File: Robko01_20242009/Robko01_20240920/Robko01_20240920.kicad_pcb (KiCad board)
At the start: 2 copper layers, 178.8 x 143.8 mm, 70 parts, among them J1 Conn_01x04_Pin, J10 Motors, J11 Motors, J12 Conn_01x04_Pin, J13 Conn_01x02_Pin, J14 Conn_01x04_Pin, J15 Conn_01x02_Pin, J16 Conn_01x04_Pin, J17 Conn_01x02_Male, J18 Conn_01x02_Male, J19 Conn_01x01_Pin, J19 Conn_01x02_Male, J2 Conn_01x02_Pin, J20 Conn_01x01_Pin, J20 Conn_01x02_Male, J21 Conn_01x19_Pin, J22 Conn_01x19_Pin, J23 Conn_01x06_Pin, J24 Conn_01x04_Pin, J25 Conn_01x04_Pin, J26 Conn_01x04_Pin, J27 Conn_01x06_Pin, J28 Conn_01x02_Male, J29 Conn_01x07_Pin, J3 Conn_01x02_Pin, J30 Conn_01x02_Male, J31 Conn_01x02_Male, J4 Conn_01x04_Pin, J5 Conn_01x02_Pin, J6 Conn_01x04_Pin, J7 Conn_01x02_Male, J8 Conn_01x02_Pin, J9 Motors, K2 G5V-2, SW1 SW_DIP_x04, SW2 SW_DIP_x04, SW3 SW_DIP_x04, SW4 SW_DIP_x04, SW5 SW_DIP_x04, SW7 SW_DIP_x04

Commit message: Add more improvements
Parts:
- removed J17, J18, J19, J31: Conn_01x02_Male, Connector_PinHeader_2.54mm:PinHeader_1x02_P2.54mm_Vertical
- removed J19: Conn_01x01_Pin, Connector_PinHeader_2.54mm:PinHeader_1x01_P2.54mm_Vertical
- removed the J20 at (68.0, 108.8)
- added C1: 100nF, Capacitor_THT:C_Disc_D7.5mm_W2.5mm_P5.00mm, F.Cu at (65.3, 113.5)
- added C2: 100nF, Capacitor_THT:C_Disc_D7.5mm_W2.5mm_P5.00mm, F.Cu at (65.3, 118.5)
- added RN1: R_Network04, Resistor_THT:R_Array_SIP5, F.Cu at (107.4, 28.5)
- added U1: LM7805_TO220, Package_TO_SOT_THT:TO-220F-3_Horizontal_TabDown, F.Cu at (70.5, 113.5)
- J30: footprint Connector_PinHeader_2.54mm:PinHeader_1x02_P2.54mm_Vertical -> Connector_PinHeader_2.54mm:PinHeader_1x02_P2.54mm_Horizontal
- moved J30 2.54 mm to (194.6, 106.5), turned to -90 degrees
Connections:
- J21 pad 1: unconnected-(J21-Pin_1-Pad1) -> +3.3V
- J30 pad 1: GRIPPER_2 -> GRIPPER_1
- J30 pad 2: GRIPPER_1 -> GRIPPER_2
- K2 pad 4: Net-(J17-Pin_1) -> GND
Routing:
- net +3.3V: track 0.00 -> 96.9 mm, vias 0 -> 1
- net Net-(J17-Pin_1): track 23.5 -> 0.00 mm
- net VCC: track 276.2 -> 270.7 mm
- net GPIO34: track 82.9 -> 86.6 mm
- net GPIO39: track 82.1 -> 85.8 mm
- net GPIO36: track 81.1 -> 84.8 mm
- net GPIO35: track 83.0 -> 86.7 mm
- net +5V: track 465.3 -> 468.3 mm
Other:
- board text removed: "D-SUN"
- board text removed: "MINI-360"

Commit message: Add E-Stop
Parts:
- added J17: Conn_01x02_Male, Connector_Phoenix_MSTB:PhoenixContact_MSTBA_2,5_2-G-5,08_1x02_P5.08mm_Horizontal, F.Cu at (45.0, 116.0)
- moved J20 50.9 mm to (86.0, 83.6), turned to 90 degrees
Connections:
- net VCC renamed MC_POWER
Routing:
- net MC_POWER: track 270.7 -> 302.0 mm
- net GND: vias 174 -> 176

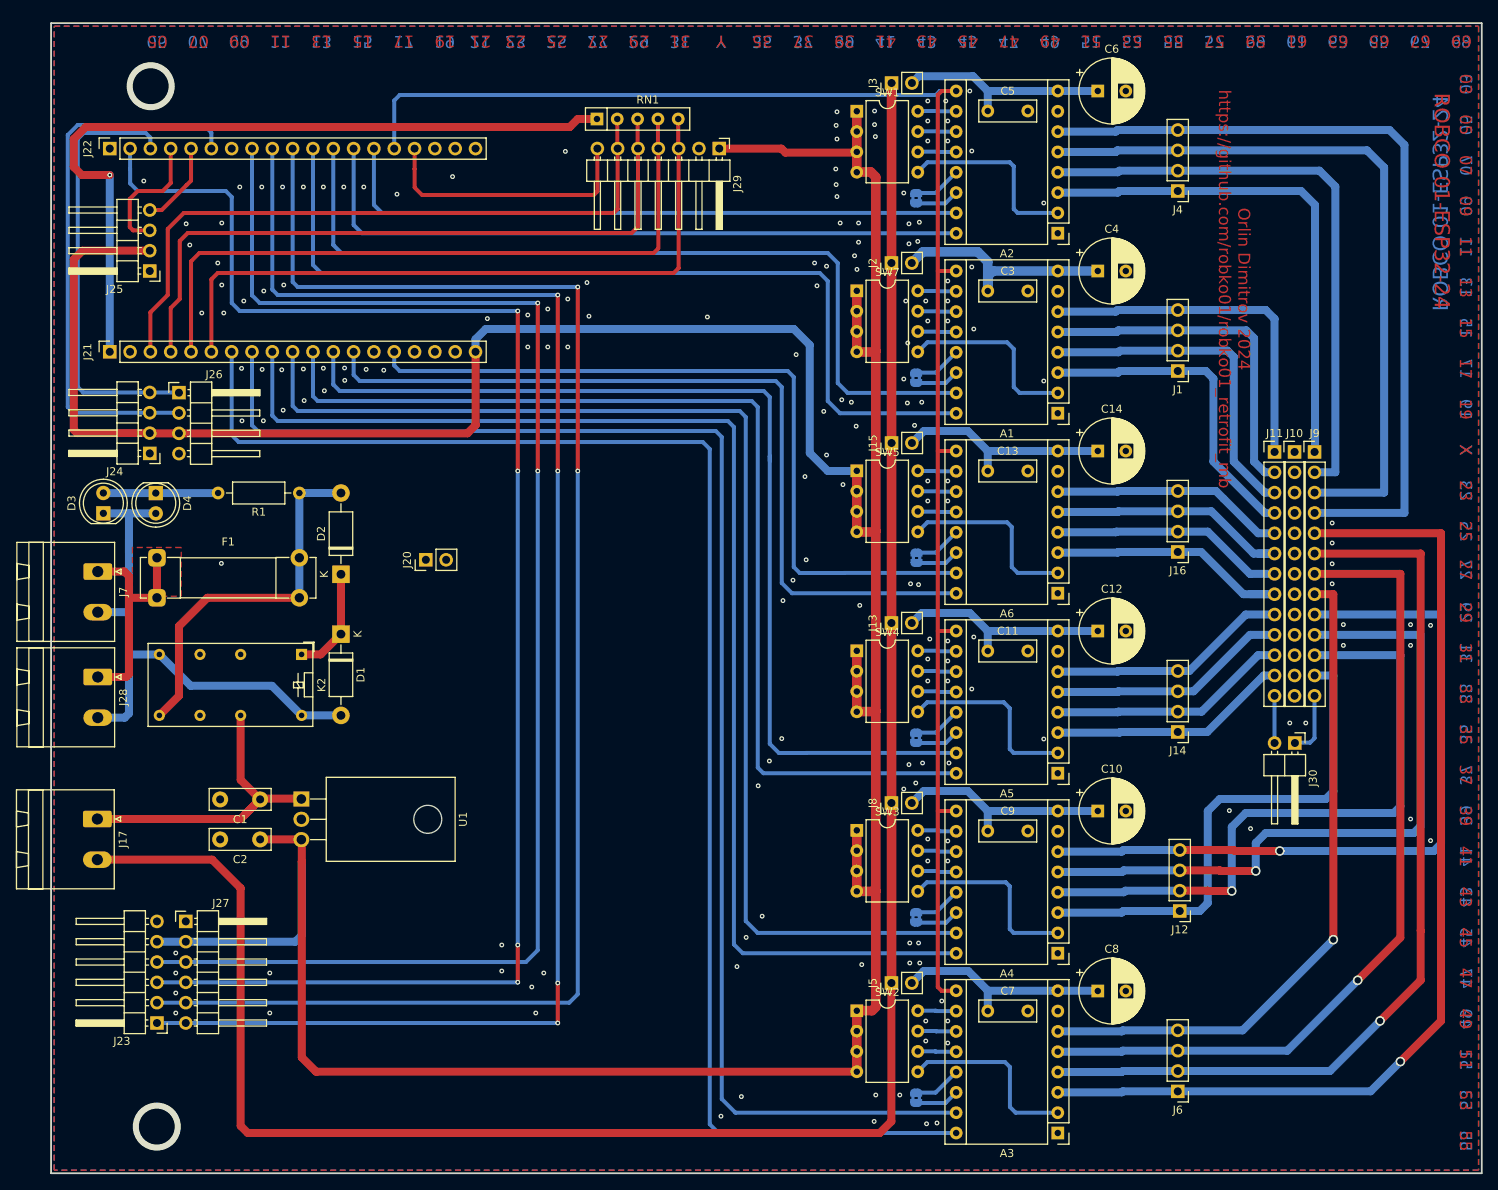
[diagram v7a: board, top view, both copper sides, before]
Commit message: Add E-Stop
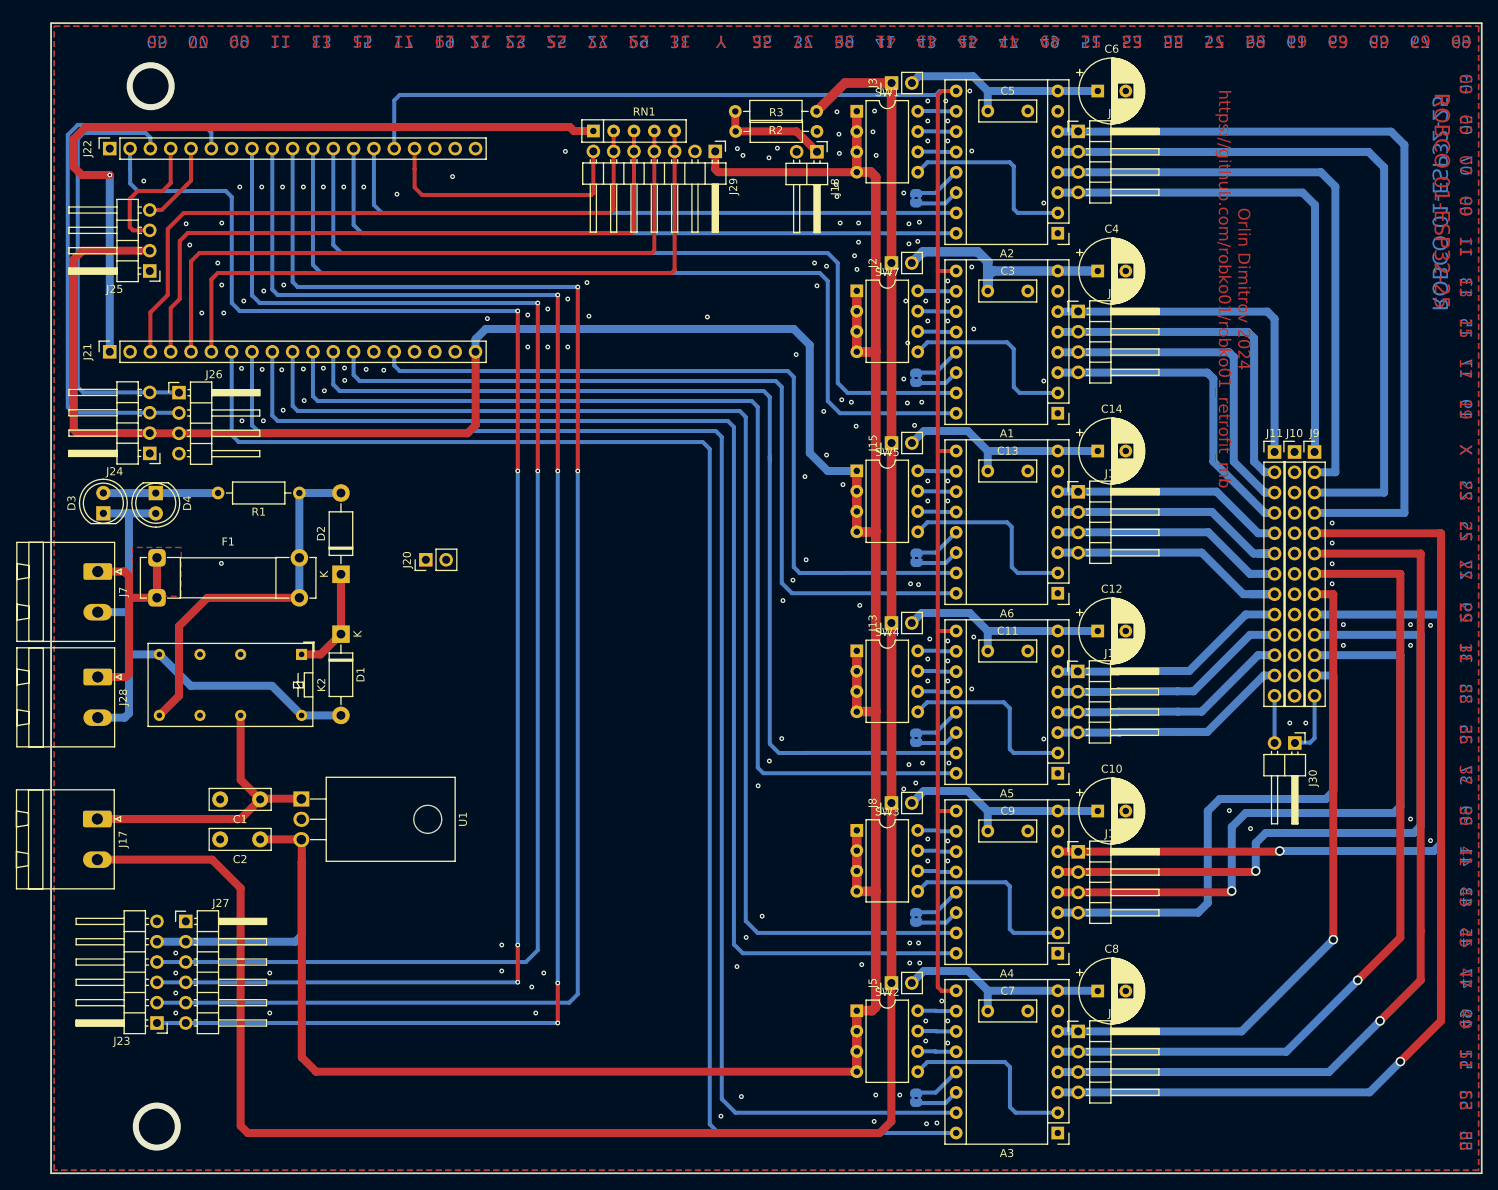
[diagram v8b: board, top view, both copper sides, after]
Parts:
- added J18: Conn_01x02_Male, Connector_PinHeader_2.54mm:PinHeader_1x02_P2.54mm_Horizontal, F.Cu at (134.9, 32.6)
- added R2: 51k, Resistor_THT:R_Axial_DIN0207_L6.3mm_D2.5mm_P10.16mm_Horizontal, F.Cu at (134.8, 27.6)
- added R3: 15k, Resistor_THT:R_Axial_DIN0207_L6.3mm_D2.5mm_P10.16mm_Horizontal, F.Cu at (124.7, 30.1)
- J1, J12, J14, J16, J4, J6: footprint Connector_PinHeader_2.54mm:PinHeader_1x04_P2.54mm_Vertical -> Connector_PinHeader_2.54mm:PinHeader_1x04_P2.54mm_Horizontal
- moved J12 14.7 mm to (167.6, 120.1), turned to 0 degrees
- moved J14 14.6 mm to (167.5, 97.5), turned to 0 degrees
- moved J16 14.5 mm to (167.6, 75.1), turned to 0 degrees
- moved J6 14.5 mm to (167.6, 142.6), turned to 0 degrees
- moved J1 14.5 mm to (167.6, 52.5), turned to 0 degrees
- moved J4 14.5 mm to (167.6, 30.1), turned to 0 degrees
- moved RN1 1.57 mm to (107.0, 30.0)
- moved J29 0.62 mm to (122.2, 32.5)
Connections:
- J1 pad 1: Net-(A1-1B) -> Net-(A1-2B)
- J1 pad 2: Net-(A1-1A) -> Net-(A1-2A)
- J1 pad 3: Net-(A1-2A) -> Net-(A1-1A)
- J1 pad 4: Net-(A1-2B) -> Net-(A1-1B)
- J12 pad 1: Net-(A4-1B) -> Net-(A4-2B)
- J12 pad 2: Net-(A4-1A) -> Net-(A4-2A)
- J12 pad 3: Net-(A4-2A) -> Net-(A4-1A)
- J12 pad 4: Net-(A4-2B) -> Net-(A4-1B)
- J14 pad 1: Net-(A5-1B) -> Net-(A5-2B)
- J14 pad 2: Net-(A5-1A) -> Net-(A5-2A)
- J14 pad 3: Net-(A5-2A) -> Net-(A5-1A)
- J14 pad 4: Net-(A5-2B) -> Net-(A5-1B)
- J16 pad 1: Net-(A6-1B) -> Net-(A6-2B)
- J16 pad 2: Net-(A6-1A) -> Net-(A6-2A)
- J16 pad 3: Net-(A6-2A) -> Net-(A6-1A)
- J16 pad 4: Net-(A6-2B) -> Net-(A6-1B)
- J17 pad 2: MC_POWER -> unconnected-(J17-Pin_2-Pad2)
- J4 pad 1: Net-(A2-1B) -> Net-(A2-2B)
- J4 pad 2: Net-(A2-1A) -> Net-(A2-2A)
- J4 pad 3: Net-(A2-2A) -> Net-(A2-1A)
- J4 pad 4: Net-(A2-2B) -> Net-(A2-1B)
- J6 pad 1: Net-(A3-1B) -> Net-(A3-2B)
- J6 pad 2: Net-(A3-1A) -> Net-(A3-2A)
- J6 pad 3: Net-(A3-2A) -> Net-(A3-1A)
- J6 pad 4: Net-(A3-2B) -> Net-(A3-1B)
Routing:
- net Net-(J18-Pin_1): track 0.00 -> 13.7 mm
- net MC_POWER: track 302.0 -> 310.2 mm
- net +5V: track 468.3 -> 470.9 mm
- net GPIO36: track 84.8 -> 82.9 mm
- net GPIO35: track 86.7 -> 84.9 mm
- net GPIO34: track 86.6 -> 84.8 mm
- net GPIO39: track 85.8 -> 84.2 mm
- net GPIO15: track 33.6 -> 32.9 mm
- net +3.3V: track 96.9 -> 96.3 mm
- net GND: vias 176 -> 179
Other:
- board text added: "ROBCO 01-ESP32-25"
- board text removed: "ROBCO 01-ESP32-24"
